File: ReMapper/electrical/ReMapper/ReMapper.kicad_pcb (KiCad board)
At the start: 2 copper layers, 3 parts, among them U1 ESP32-S3-WROOM-1-N8R8, U2 SC0914_13_, U3 ESP32-S3-WROOM-1

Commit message: more work on schematic
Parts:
- added D2: ESD, Diode_SMD:D_SOD-523, F.Cu at (133.2, 76.4)
- added D3: ESD, Diode_SMD:D_SOD-523, F.Cu at (133.2, 78.8)
- added D4: ESD, Diode_SMD:D_SOD-523, F.Cu at (149.7, 74.5)
- added D5: ESD, Diode_SMD:D_SOD-523, F.Cu at (149.7, 77.0)
- added J1: QSPI_Debug, Connector_PinHeader_1.00mm:PinHeader_1x08_P1.00mm_Vertical, F.Cu at (119.9, 76.7)
- added J2: USB_IN, footprints:USBA_Female, F.Cu at (127.2, 67.2)
- added J3: USB__IN_Debug, Connector_PinHeader_1.00mm:PinHeader_1x02_P1.00mm_Vertical, F.Cu at (133.0, 81.6)
- added J4: ESP_UART0, Connector_PinHeader_1.00mm:PinHeader_1x04_P1.00mm_Vertical, F.Cu at (167.5, 59.0)
- added J5: USB_OUT, footprints:USBA_Female, F.Cu at (156.8, 65.4)
- added JP1: PFM Mode, Jumper:SolderJumper-2_P1.3mm_Open_Pad1.0x1.5mm, F.Cu at (133.8, 86.2)
- added JP2: GND_SHIELD, Jumper:SolderJumper-2_P1.3mm_Open_Pad1.0x1.5mm, F.Cu at (133.8, 89.8)
- added JP3: GND_SHIELD, Jumper:SolderJumper-2_P1.3mm_Open_Pad1.0x1.5mm, F.Cu at (153.6, 75.1)
- added U4: RT6150B-33GQW, footprints:RT6150B-33GQW, F.Cu at (100.1, 88.9)
- U2: value SC0914_13_ -> RP2040
- U3: value ESP32-S3-WROOM-1 -> W25Q128JVE; footprint RF_Module:ESP32-S3-WROOM-1 -> Package_SON:WSON-8-1EP_8x6mm_P1.27mm_EP3.4x4.3mm
- moved U2 58.5 mm to (126.7, 79.8)
- moved U3 13.3 mm to (126.8, 88.2)
- moved U1 9.35 mm to (108.0, 72.8)
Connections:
- U1 pad 1: Net-(U1-GND-Pad1) -> GND
- U1 pad 10: unconnected-(U1-IO17-Pad10) -> /QSPI_CS_esp
- U1 pad 13: unconnected-(U1-IO19-Pad13) -> /USB_OUT_D+
- U1 pad 14: unconnected-(U1-IO20-Pad14) -> /USB_OUT_D-
- U1 pad 19: unconnected-(U1-IO11-Pad19) -> /QSPI_CLK_esp
- U1 pad 2: unconnected-(U1-3V3-Pad2) -> /3.3V
- U1 pad 20: unconnected-(U1-IO12-Pad20) -> /QSPI_IO0_esp
- U1 pad 21: unconnected-(U1-IO13-Pad21) -> /QSPI_IO1_esp
- U1 pad 22: unconnected-(U1-IO14-Pad22) -> /QSPI_IO2_esp
- U1 pad 23: unconnected-(U1-IO21-Pad23) -> /QSPI_IO3_esp
- U1 pad 3: unconnected-(U1-EN-Pad3) -> Net-(U1-EN)
- U1 pad 36: unconnected-(U1-RXD0-Pad36) -> /ESP_TXDO
- U1 pad 37: unconnected-(U1-TXD0-Pad37) -> /ESP_RXDO
- U1 pad 4: unconnected-(U1-IO4-Pad4) -> /SPI2_MOSI
- U1 pad 40: Net-(U1-GND-Pad1) -> GND
- U1 pad 41_1: Net-(U1-GND-Pad1) -> GND
- U1 pad 41_2: Net-(U1-GND-Pad1) -> GND
- U1 pad 41_3: Net-(U1-GND-Pad1) -> GND
- U1 pad 41_4: Net-(U1-GND-Pad1) -> GND
- U1 pad 41_5: Net-(U1-GND-Pad1) -> GND
- U1 pad 41_6: Net-(U1-GND-Pad1) -> GND
- U1 pad 41_7: Net-(U1-GND-Pad1) -> GND
- U1 pad 41_8: Net-(U1-GND-Pad1) -> GND
- U1 pad 41_9: Net-(U1-GND-Pad1) -> GND
- U1 pad 5: unconnected-(U1-IO5-Pad5) -> /SPI2_MISO
- U1 pad 6: unconnected-(U1-IO6-Pad6) -> /SPI2_CLK
- U1 pad 7: unconnected-(U1-IO7-Pad7) -> /SPI2_CS
- U3 pad 1: Net-(U3-GND-Pad1) -> /QSPI_CS_esp
- U3 pad 2: unconnected-(U3-3V3-Pad2) -> /QSPI_IO1_esp
- U3 pad 3: unconnected-(U3-EN-Pad3) -> /QSPI_IO2_esp
- U3 pad 4: unconnected-(U3-IO4-Pad4) -> GND
- U3 pad 5: unconnected-(U3-IO5-Pad5) -> /QSPI_IO0_esp
- U3 pad 6: unconnected-(U3-IO6-Pad6) -> /QSPI_CLK_esp
- U3 pad 7: unconnected-(U3-IO7-Pad7) -> /QSPI_IO3_esp
- U3 pad 8: unconnected-(U3-IO15-Pad8) -> /3.3V

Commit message: schematic first draft, onto layout
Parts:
- added C1: 22uf, Capacitor_SMD:C_0603_1608Metric, F.Cu at (118.4, 85.8)
- added C10: 100nf, Capacitor_SMD:C_0603_1608Metric, F.Cu at (122.5, 93.3)
- added C11: 15 pF, Capacitor_SMD:C_0603_1608Metric, F.Cu at (122.5, 95.8)
- added C12: 15 pF, Capacitor_SMD:C_0603_1608Metric, F.Cu at (122.5, 98.3)
- added C13: 2.2uf, Capacitor_SMD:C_0603_1608Metric, F.Cu at (126.5, 85.8)
- added C2: 0.1uf, Capacitor_SMD:C_0603_1608Metric, F.Cu at (118.4, 88.3)
- added C3: 1uf, Capacitor_SMD:C_0603_1608Metric, F.Cu at (118.4, 90.8)
- added C4: 2.2uf, Capacitor_SMD:C_0603_1608Metric, F.Cu at (118.4, 93.3)
- added C5: 100nf, Capacitor_SMD:C_0603_1608Metric, F.Cu at (118.4, 95.8)
- added C6: 47uF, Capacitor_SMD:C_0603_1608Metric, F.Cu at (118.4, 98.3)
- added C7: 47uF, Capacitor_SMD:C_0603_1608Metric, F.Cu at (122.5, 85.8)
- added C8: 47uF, Capacitor_SMD:C_0603_1608Metric, F.Cu at (122.5, 88.3)
- added C9: 2.2uf, Capacitor_SMD:C_0603_1608Metric, F.Cu at (122.5, 90.8)
- added D1: D_Schottky, Diode_SMD:D_SOD-123, F.Cu at (98.2, 98.0)
- added D6: LED 33V, LED_SMD:LED_0603_1608Metric, F.Cu at (114.4, 88.4)
- added D7: LED USB VIN, LED_SMD:LED_0603_1608Metric, F.Cu at (114.4, 91.0)
- added D8: LED RP5, LED_SMD:LED_0603_1608Metric, F.Cu at (114.4, 93.6)
- added D9: LED RP5, LED_SMD:LED_0603_1608Metric, F.Cu at (114.4, 96.1)
- added J6: USB_OUT_Debug, Connector_PinHeader_1.00mm:PinHeader_1x02_P1.00mm_Vertical, F.Cu at (113.4, 81.9)
- added JP4: RP_RUN, Jumper:SolderJumper-2_P1.3mm_Open_Pad1.0x1.5mm, F.Cu at (136.6, 69.3)
- added JP5: RP_crystal, Jumper:SolderJumper-2_P1.3mm_Open_Pad1.0x1.5mm, F.Cu at (136.6, 72.8)
- added L1: 2.2uH, Inductor_SMD:L_0603_1608Metric, F.Cu at (126.5, 88.3)
- added R1: 10k, Resistor_SMD:R_0603_1608Metric, F.Cu at (126.5, 90.8)
- added R2: 100k, Resistor_SMD:R_0603_1608Metric, F.Cu at (126.5, 93.3)
- added R3: 1k, Resistor_SMD:R_0603_1608Metric, F.Cu at (126.5, 95.8)
- added R4: 1k, Resistor_SMD:R_0603_1608Metric, F.Cu at (126.5, 98.3)
- added R5: 400, Resistor_SMD:R_0603_1608Metric, F.Cu at (130.5, 85.8)
- added R6: 800, Resistor_SMD:R_0603_1608Metric, F.Cu at (130.5, 88.3)
- added R7: 400, Resistor_SMD:R_0603_1608Metric, F.Cu at (130.5, 90.8)
- added R8: 400, Resistor_SMD:R_0603_1608Metric, F.Cu at (130.5, 93.3)
- added S1: SKRPABE010, footprints:push_button_SKRPABE010, F.Cu at (109.0, 89.5)
- added S2: SKRPABE010, footprints:push_button_SKRPABE010, F.Cu at (109.0, 94.2)
- added U5: W25Q128JVE, Package_SON:WSON-8-1EP_8x6mm_P1.27mm_EP3.4x4.3mm, F.Cu at (137.8, 95.8)
- added Y1: 12MHZ, Crystal:Crystal_HC49-4H_Vertical, F.Cu at (99.4, 83.7)
- J3: value USB__IN_Debug -> USB_IN_Debug
- moved U4 50.6 mm to (137.5, 54.8)
- moved J5 33.3 mm to (125.4, 76.6)
- moved J4 32.7 mm to (139.7, 76.1)
- moved U2 28.9 mm to (100.4, 91.7)
- moved JP1 27.7 mm to (136.6, 58.6)
- moved JP2 27.7 mm to (136.6, 62.2)
- moved J1 27.5 mm to (140.5, 58.4)
- moved J3 23.0 mm to (110.0, 81.9)
- moved JP3 19.4 mm to (136.6, 65.7)
- moved D4 14.8 mm to (136.3, 80.7)
- moved D5 14.8 mm to (136.3, 83.2)
- moved U3 10.9 mm to (137.8, 88.3)
- moved U1 6.74 mm to (106.2, 66.3)
- moved J2 6.74 mm to (125.4, 60.7)
- moved D2 3.13 mm to (136.3, 75.8)
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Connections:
- U1 pad 12: unconnected-(U1-IO8-Pad12) -> /IO8_esp
- U2 pad 1: unconnected-(U2-IOVDD-Pad1) -> /3.3V
- U2 pad 10: unconnected-(U2-IOVDD__1-Pad10) -> /3.3V
- U2 pad 19: unconnected-(U2-TESTEN-Pad19) -> GND
- U2 pad 20: unconnected-(U2-XIN-Pad20) -> /XIN_rp
- U2 pad 21: unconnected-(U2-XOUT-Pad21) -> /XOUT_rp
- U2 pad 22: unconnected-(U2-IOVDD__2-Pad22) -> /3.3V
- U2 pad 23: unconnected-(U2-DVDD-Pad23) -> Net-(U2-DVDD)
- U2 pad 26: unconnected-(U2-RUN-Pad26) -> Net-(JP4-B)
- U2 pad 27: unconnected-(U2-GPIO16-Pad27) -> /SPI2_MOSI
- U2 pad 28: unconnected-(U2-GPIO17-Pad28) -> /SPI2_CS
- U2 pad 29: unconnected-(U2-GPIO18-Pad29) -> /SPI2_CLK
- U2 pad 30: unconnected-(U2-GPIO19-Pad30) -> /SPI2_MISO
- U2 pad 33: unconnected-(U2-IOVDD__3-Pad33) -> /3.3V
- U2 pad 42: unconnected-(U2-IOVDD__4-Pad42) -> /3.3V
- U2 pad 43: unconnected-(U2-ADC_AVDD-Pad43) -> /3.3V
- U2 pad 44: unconnected-(U2-VREG_VIN-Pad44) -> /3.3V
- U2 pad 45: unconnected-(U2-VREG_VOUT-Pad45) -> Net-(U2-DVDD)
- U2 pad 46: unconnected-(U2-USB_DM-Pad46) -> /USB_OUT_D+
- U2 pad 47: unconnected-(U2-USB_DP-Pad47) -> /USB_OUT_D-
- U2 pad 48: unconnected-(U2-USB_VDD-Pad48) -> /3.3V
- U2 pad 49: unconnected-(U2-IOVDD__5-Pad49) -> /3.3V
- U2 pad 50: unconnected-(U2-DVDD__1-Pad50) -> Net-(U2-DVDD)
- U2 pad 51: unconnected-(U2-QSPI_SD3-Pad51) -> /QSPI_IO3_rp
- U2 pad 52: unconnected-(U2-QSPI_SCLK-Pad52) -> /QSPI_CLK_rp
- U2 pad 53: unconnected-(U2-QSPI_SD0-Pad53) -> /QSPI_IO0_rp
- U2 pad 54: unconnected-(U2-QSPI_SD2-Pad54) -> /QSPI_IO2_rp
- U2 pad 55: unconnected-(U2-QSPI_SD1-Pad55) -> /QSPI_IO1_rp
- U2 pad 56: unconnected-(U2-QSPI_SS_N-Pad56) -> /QSPI_CS_rp
- U2 pad 57: unconnected-(U2-GND-Pad57) -> GND
- U2 pad 7: unconnected-(U2-GPIO5-Pad7) -> /GPIO5_rp

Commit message: started layout
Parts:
- J5: footprint footprints:USBA_Female -> Connector_PinHeader_1.00mm:PinHeader_1x04_P1.00mm_Vertical
- moved J2 69.0 mm to (56.5, 62.8), turned to -90 degrees
- moved JP2 67.3 mm to (70.0, 72.0), turned to 90 degrees
- moved D1 48.2 mm to (69.5, 59.2)
- moved J5 44.8 mm to (168.0, 90.5), turned to 90 degrees
- moved U1 17.9 mm to (98.8, 50.0)

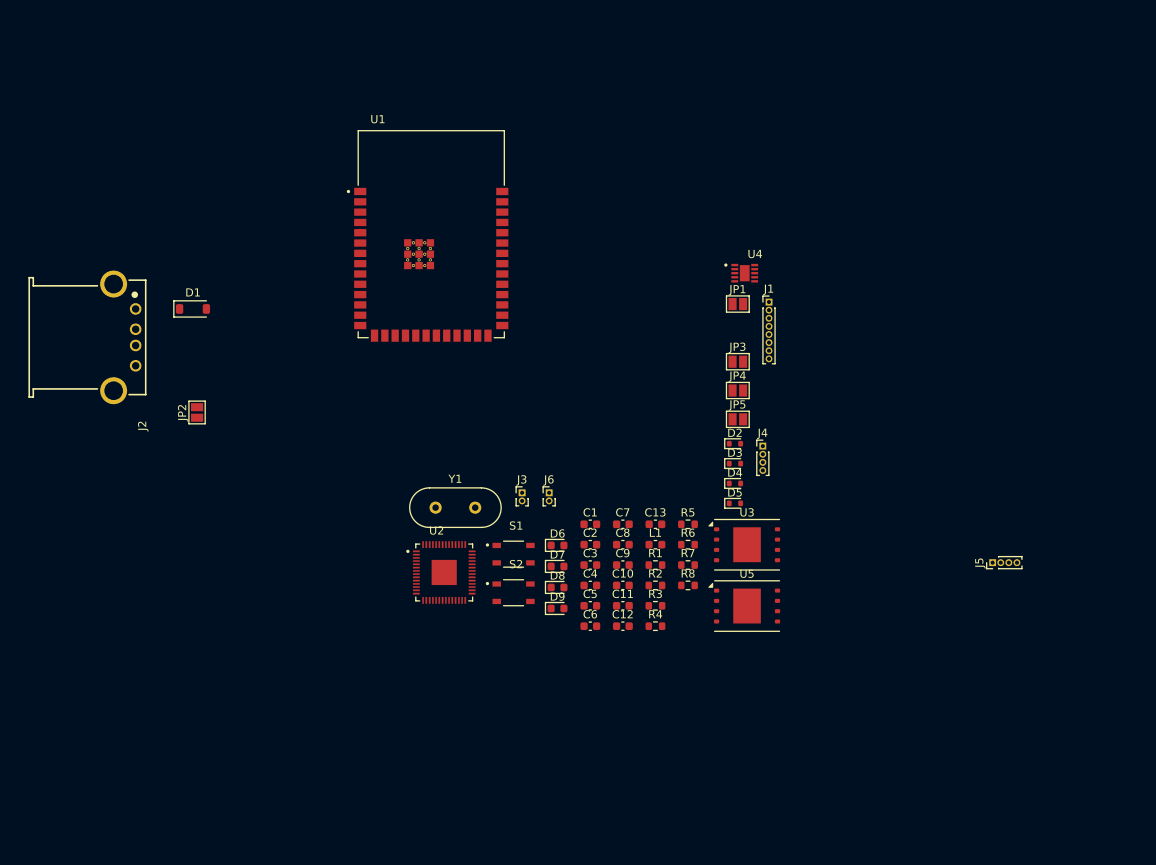
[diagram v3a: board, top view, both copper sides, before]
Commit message: split he layout a little
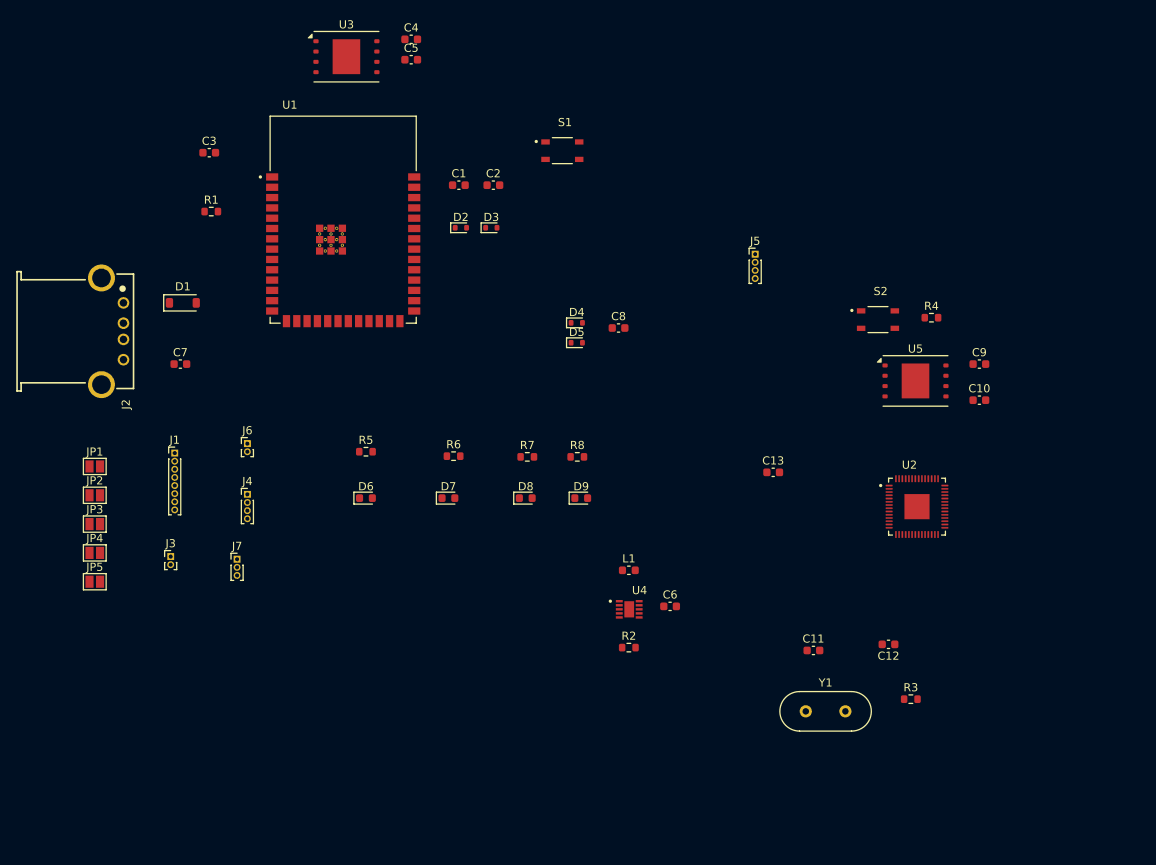
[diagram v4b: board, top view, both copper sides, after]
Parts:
- added J7: SWD, Connector_PinHeader_1.00mm:PinHeader_1x03_P1.00mm_Vertical, F.Cu at (74.9, 90.1)
- moved JP1 81.7 mm to (57.4, 78.7)
- moved JP3 81.7 mm to (57.4, 85.8)
- moved JP4 81.7 mm to (57.4, 89.3)
- moved JP5 81.7 mm to (57.4, 92.8)
- moved U3 77.8 mm to (88.4, 28.2)
- moved J1 75.5 mm to (67.2, 77.0)
- moved C4 70.8 mm to (96.4, 26.0)
- moved C5 70.8 mm to (96.4, 28.5)
- moved R1 69.9 mm to (71.8, 47.2)
- moved C3 69.2 mm to (71.5, 40.0)
- moved J4 63.8 mm to (76.2, 82.1)
- moved U2 58.8 mm to (158.7, 83.6)
- moved C7 58.0 mm to (67.9, 66.0)
- moved S2 56.1 mm to (153.9, 60.6)
- moved Y1 52.0 mm to (145.0, 108.8)
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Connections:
- U2 pad 24: unconnected-(U2-SWCLK-Pad24) -> /SWCLK_rp
- U2 pad 25: unconnected-(U2-SWDIO-Pad25) -> /SWDIO_rp
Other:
- copper layers 2 -> 4

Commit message: rough placements
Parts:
- moved JP3 129.2 mm to (182.8, 116.5)
- moved USB_IN1 112.3 mm to (178.8, 98.2)
- moved JP4 109.1 mm to (166.3, 96.4)
- moved JP5 109.1 mm to (166.1, 101.4)
- moved ESP_QSPI1 106.1 mm to (172.5, 90.5), turned to 180 degrees
- moved RP_SWD1 104.6 mm to (179.5, 88.9)
- moved USB_OUT1 104.3 mm to (180.2, 83.2)
- moved ESP_UART0 97.1 mm to (172.5, 94.8)
- moved S1 82.1 mm to (145.7, 115.9)
- moved C3 67.2 mm to (107.5, 96.7)
- moved J5 64.7 mm to (183.5, 99.2)
- moved C1 64.3 mm to (146.1, 91.0)
- moved C2 64.3 mm to (150.4, 91.0)
- moved D2 64.3 mm to (146.4, 96.3)
- moved D3 64.3 mm to (150.1, 96.3)
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- renumbered D6 to 33V_led1, J1 to ESP_QSPI1, J4 to ESP_UART0, J7 to RP_SWD1, J3 to USB_IN1, J6 to USB_OUT1, D7 to USB_led1, D9 to esp_led1, D8 to rp_led1

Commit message: layout half done, might needs a remake
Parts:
- moved ESP_UART0 42.0 mm to (131.8, 105.0), turned to 90 degrees
- moved C4 22.0 mm to (123.8, 103.5)
- moved C5 22.0 mm to (123.8, 106.0)
- moved D2 16.6 mm to (156.5, 109.5), turned to 180 degrees
- moved C1 15.4 mm to (148.2, 106.2)
- moved D3 11.8 mm to (156.5, 106.2)
- moved C13 8.62 mm to (152.5, 107.8)
- moved J5 7.98 mm to (179.2, 106.0)
- moved R4 7.72 mm to (156.8, 83.2)
- moved U3 7.45 mm to (112.4, 86.2)
- moved 33V_led1 6.43 mm to (118.0, 115.2)
- moved R5 6.43 mm to (118.0, 112.6)
- moved U1 4.28 mm to (133.5, 91.3), turned to -90 degrees
- moved C2 4.24 mm to (150.8, 95.2)
- moved R6 4.16 mm to (125.1, 112.6)
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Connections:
- U2 pad 46: /USB_OUT_D+ -> /USB_IN_D+
- U2 pad 47: /USB_OUT_D- -> /USB_IN_D-
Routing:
- net GND: track 0.00 -> 99.5 mm, vias 0 -> 42
- net Net-(R4-Pad1): track 0.00 -> 53.8 mm, vias 0 -> 2
- net /USB_VIN: track 0.00 -> 52.9 mm
- net Net-(U1-EN): track 0.00 -> 49.1 mm, vias 0 -> 2
- net /3.3V: track 0.00 -> 38.8 mm, vias 0 -> 14
- net /IO8_esp: track 0.00 -> 35.4 mm, vias 0 -> 2
- net /GPIO5_rp: track 0.00 -> 31.4 mm, vias 0 -> 2
- net /SWCLK_rp: track 0.00 -> 30.9 mm, vias 0 -> 2
- net /QSPI_CS_esp: track 0.00 -> 27.1 mm, vias 0 -> 2
- net /XIN_rp: track 0.00 -> 24.0 mm, vias 0 -> 2
- net /USB_OUT_D+: track 0.00 -> 23.0 mm
- net Net-(JP4-B): track 0.00 -> 22.8 mm, vias 0 -> 2
- net /USB_OUT_D-: track 0.00 -> 22.4 mm
- net /QSPI_IO1_esp: track 0.00 -> 20.0 mm, vias 0 -> 2
- net /XOUT_rp: track 0.00 -> 19.1 mm, vias 0 -> 2
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- added copper zone on In2.Cu, net /3.3V
- added copper zone on In1.Cu, net GND
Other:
- board text added: "3.3V"
- board text added: "ESP"
- board text added: "ESP_UART"
- board text added: "QSPI_ESP"
- board text added: "RP"
- board text added: "USBVIN"
- board text added: "USB_IN"
- board text added: "USB_OUT"
- board text added: "rp_SWD"

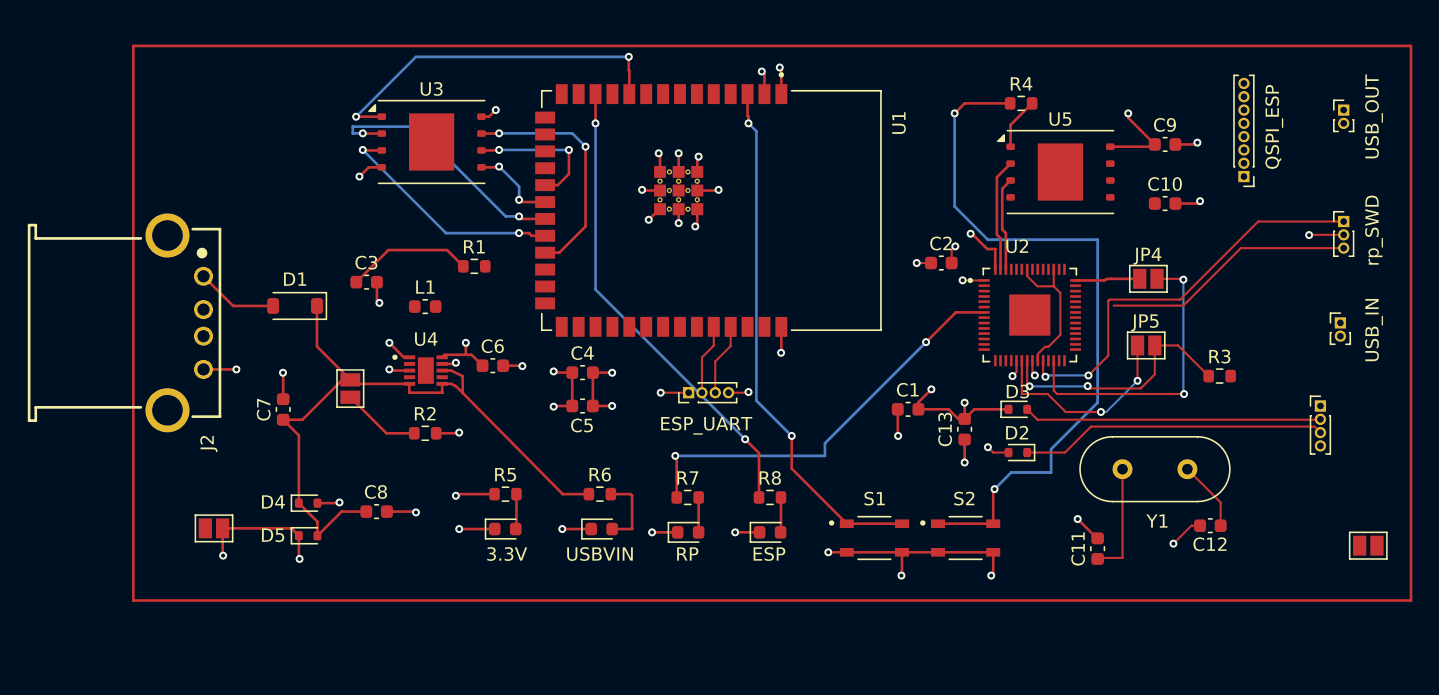
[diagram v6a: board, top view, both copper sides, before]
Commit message: passing DRC
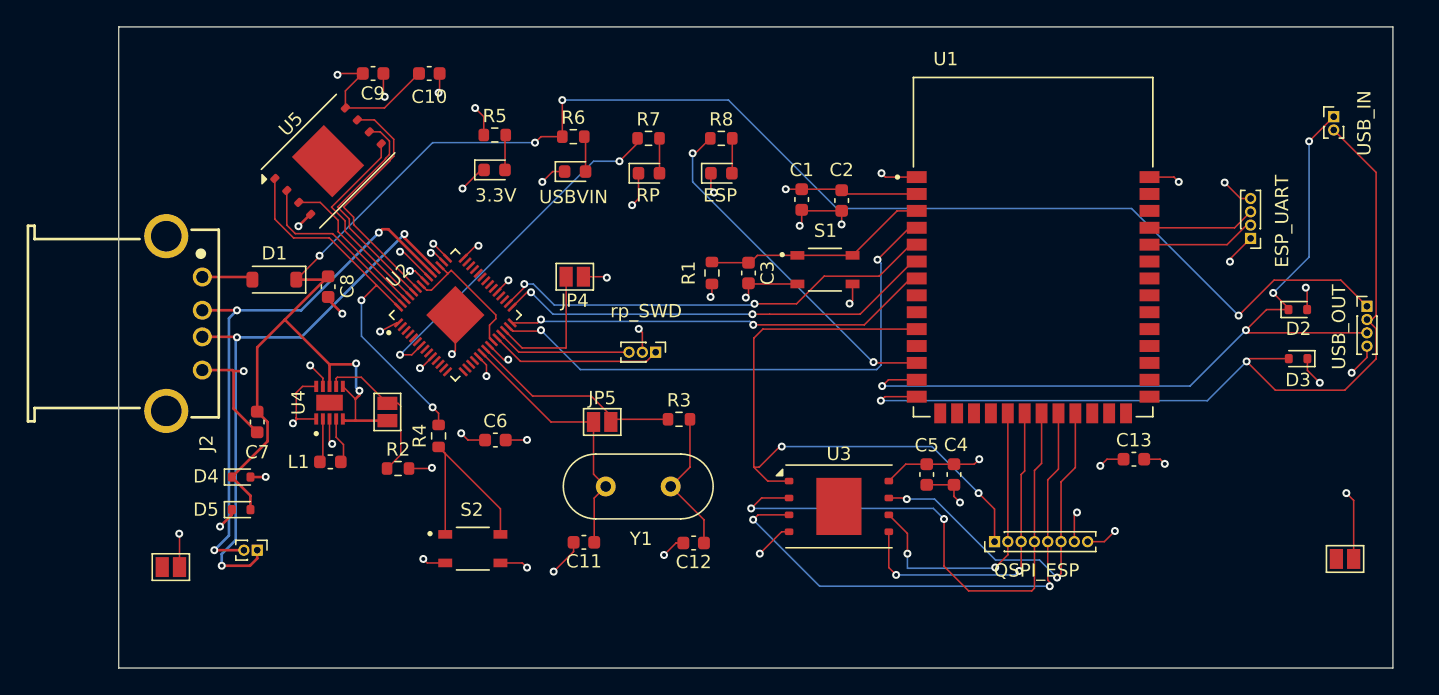
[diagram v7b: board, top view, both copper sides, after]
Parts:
- moved USB_IN1 83.2 mm to (99.3, 116.8), turned to -90 degrees
- moved C9 59.8 mm to (108.0, 81.0)
- moved C10 56.2 mm to (112.2, 81.0)
- moved U5 55.1 mm to (104.6, 87.6), turned to 45 degrees
- moved RP_SWD1 52.7 mm to (129.3, 102.0), turned to -90 degrees
- moved R4 50.4 mm to (113.0, 108.2), turned to 90 degrees
- moved ESP_UART0 43.8 mm to (174.0, 93.4), turned to 180 degrees
- moved U2 43.2 mm to (114.2, 99.2), turned to 45 degrees
- moved JP4 43.1 mm to (123.2, 96.3), turned to 180 degrees
- moved JP5 41.3 mm to (125.2, 107.2)
- moved U3 41.1 mm to (143.1, 113.5)
- moved R3 40.8 mm to (131.0, 107.0)
- moved Y1 38.9 mm to (125.5, 112.0)
- moved C12 38.9 mm to (132.1, 116.3)
- moved C11 38.6 mm to (123.9, 116.2), turned to 180 degrees
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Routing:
- net /USB_VIN: track 52.9 -> 138.3 mm, vias 0 -> 6
- net /USB_OUT_D-: track 22.4 -> 65.7 mm, vias 0 -> 2
- net /USB_IN_D+: track 0.00 -> 43.3 mm, vias 0 -> 3
- net /USB_IN_D-: track 0.00 -> 42.2 mm, vias 0 -> 3
- net /SPI2_MOSI: track 0.00 -> 41.5 mm, vias 0 -> 2
- net /USB_OUT_D+: track 23.0 -> 61.8 mm, vias 0 -> 4
- net Net-(R4-Pad1): track 53.8 -> 15.3 mm, vias 2 -> 0
- net /SPI2_MISO: track 0.00 -> 34.0 mm, vias 0 -> 2
- net /SPI2_CLK: track 0.00 -> 33.2 mm, vias 0 -> 2
- net /SPI2_CS: track 0.00 -> 32.1 mm, vias 0 -> 2
- net Net-(U1-EN): track 49.1 -> 17.0 mm, vias 2 -> 0
- net /3.3V: track 38.8 -> 63.2 mm, vias 14 -> 20
- net /QSPI_IO2_esp: track 17.8 -> 40.6 mm
- net /QSPI_IO1_esp: track 20.0 -> 42.6 mm
- net /QSPI_CS_esp: track 27.1 -> 48.5 mm
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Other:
- board outline added: 95.8 x 48.2 mm
